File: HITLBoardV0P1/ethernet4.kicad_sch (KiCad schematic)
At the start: 36 parts, among them U2 LAN8650B1-E/LMX, U3 LP38852MRX-ADJ/NOPB

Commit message: in progress, brute forced lan8650 layouts :( damn you kicad
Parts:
- renumbered C25 to C100, C1 to C76, C2 to C77, C3 to C78, C4 to C79, C5 to C80, C6 to C81, C7 to C82, C8 to C83, C9 to C84, C10 to C85, C11 to C86, C12 to C87, C13 to C88, C14 to C89, C15 to C90, C16 to C91, C17 to C92, C18 to C93, C19 to C94, C20 to C95, C21 to C96, C22 to C97, C23 to C98, C24 to C99, R1 to R25, R2 to R26, R3 to R27, R4 to R28, R5 to R29, R6 to R30, R7 to R31, R8 to R32, U2 to U8, U3 to U9, XTAL1 to XTAL4
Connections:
- net U3_DAP is gone; now on net GND: U9.9 (DAP)
- net +3V3: no longer C80.1, C81.1, C82.1, C83.1, C84.1, C85.1
- net 1V8_U2 renamed 1V8
- net 1V8: now also C80.1, C81.1, C82.1, C83.1, C84.1, C85.1
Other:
- moved on the sheet: C100, C76, C77, C78, C79, C80, C81, C82, C83, C84, C85, C86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

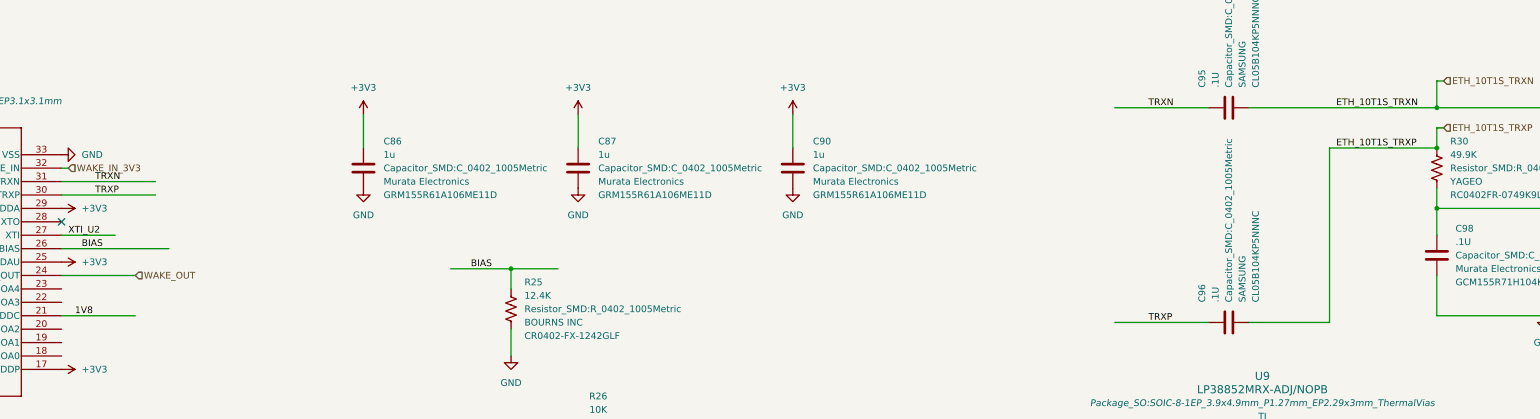
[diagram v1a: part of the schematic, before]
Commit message: MINOR UPDATES -- SWTICH ONE LAN TO SPI 5 INSTEAD OF SPI1 ON THE TMDX, SET UP LAN8650S for actual differential pair routing by changing suffix to "_DN" and "_DP" instead of "_N" or "_P" or just "N", "P"
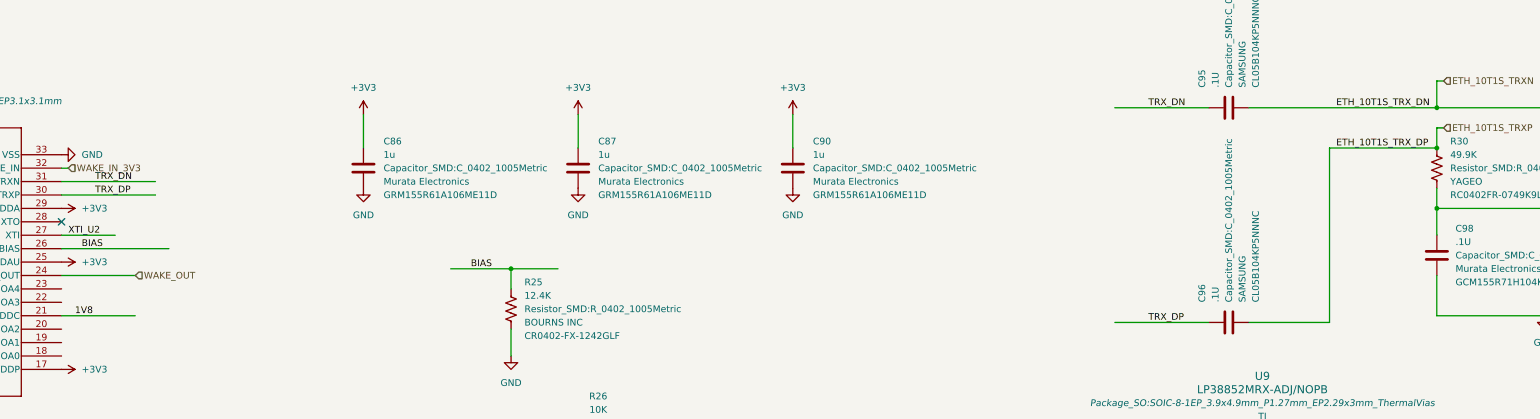
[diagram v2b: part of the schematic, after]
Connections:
- net TRXN renamed TRX_DN
- net TRXP renamed TRX_DP
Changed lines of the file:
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@@
 		)
 	)
-	(label "TRXP"
+	(label "TRX_DP"
 		(at 110.49 52.07 0)
 		(effects
@@
 		)
 	)
-	(label "ETH_10T1S_TRXN"
+	(label "ETH_10T1S_TRX_DN"
 		(at 345.44 35.56 0)
 		(effects
@@
 		)
 	)
-	(label "TRXN"
+	(label "TRX_DN"
 		(at 110.49 49.53 0)
 		(effects
@@
 		)
 	)
-	(label "TRXN"
+	(label "TRX_DN"
 		(at 309.88 35.56 0)
 		(effects
@@
 		)
 	)
-	(label "ETH_10T1S_TRXP"
+	(label "ETH_10T1S_TRX_DP"
 		(at 345.44 43.18 0)
 		(effects
@@
 		)
 	)
-	(label "TRXP"
+	(label "TRX_DP"
 		(at 309.88 76.2 0)
 		(effects
